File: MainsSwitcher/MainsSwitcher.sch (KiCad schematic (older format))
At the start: 25 parts, among them J1 SERIAL, J2 LED_STRIP, J3 SWITCHING, J4 MAINS_IN, J5 TEMP_SEN1, J6 TEMP_SEN2, K1 Relay, P1 GPIO, Q1 MOSFET_N, Q2 MCP1700T-3302E/TT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

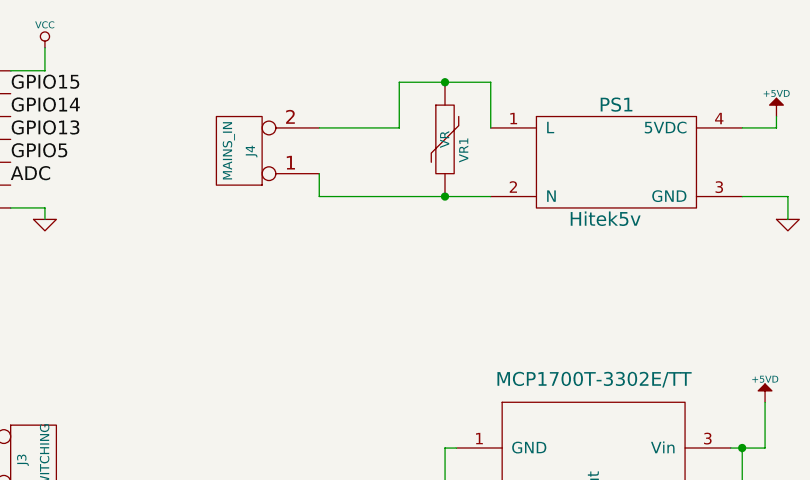
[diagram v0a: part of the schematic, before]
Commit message: Added fuseholder
Fuseholder added to the mains inlet. As ordered.
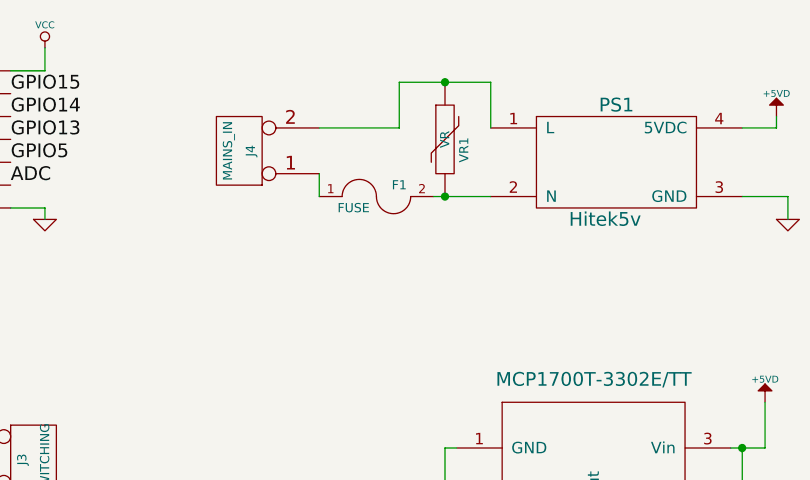
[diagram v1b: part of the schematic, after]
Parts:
- added F1: FUSE, TJS:Schurter_Fuseholder(20x5mm)0031.8211, symbol FUSE
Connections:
- net at PS1.2 (N), VR1.2: now also F1.2; no longer J4.1 (P1)
- new net: F1.1, J4.1 (P1)
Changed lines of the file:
@@
 Connection ~ 8900 850
 Connection ~ 8900 1350
-Wire Wire Line
-	8350 1350 9100 1350
 $Comp
 L +5VD #PWR028
@@
 Wire Wire Line
 	6600 5300 6600 5450
+$Comp
+L FUSE F1
+U 1 1 58B4A8B2
+P 8600 1350
+F 0 "F1" H 8700 1400 40  0000 C CNN
+F 1 "FUSE" H 8500 1300 40  0000 C CNN
+F 2 "TJS:Schurter_Fuseholder(20x5mm)0031.8211" H 8600 1350 60  0001 C CNN
+F 3 "" H 8600 1350 60  0000 C CNN
+	1    8600 1350
+	1    0    0    -1
+$EndComp
+Wire Wire Line
+	8850 1350 9100 1350
 $EndSCHEMATC

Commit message: Changes to who knows what.
Uncommitted changes to stuff. Tidying up…
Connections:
- net GND: now also U1.10 (GPIO15)
- net VCC: now also P1.6 (P6)
- removed net GPIO15: P1.6 (P6), U1.10 (GPIO15)
- net GPIO5 renamed GPIO4
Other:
- note added: "Note:\nGPIO4 and GPIO5 are swapped\n on the original part net for the \nESP8266."
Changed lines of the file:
@@
 GPIO13
 Text Label 3100 3000 0    60   ~ 0
-GPIO5
+GPIO4
 Text Label 3100 3800 0    60   ~ 0
 ADC
@@
 ADC
 Text Label 7000 1200 0    60   ~ 0
-GPIO5
+GPIO4
 Text Label 7000 1100 0    60   ~ 0
 GPIO13
 Text Label 7000 1000 0    60   ~ 0
 GPIO14
-Text Label 7000 900  0    60   ~ 0
-GPIO15
 Wire Wire Line
 	7150 800  7000 800
@@
 $EndComp
 Wire Wire Line
-	7150 700  7150 800
+	7150 700  7150 900
 Wire Wire Line
 	8450 5100 8450 5050
@@
 	6600 4250 6250 4250
 Text Label 6250 4250 0    60   ~ 0
-GPIO5
+GPIO4
 Wire Wire Line
 	6600 5300 6600 5450
@@
 Wire Wire Line
 	8850 1350 9100 1350
+$Comp
+L GND #PWR?
+U 1 1 59711544
+P 3600 2250
+F 0 "#PWR?" H 3600 2250 30  0001 C CNN
+F 1 "GND" H 3600 2180 30  0001 C CNN
+F 2 "" H 3600 2250 60  0001 C CNN
+F 3 "" H 3600 2250 60  0001 C CNN
+	1    3600 2250
+	1    0    0    -1
+$EndComp
+Wire Wire Line
+	3600 2250 3600 2200
+Wire Wire Line
+	3600 2200 3100 2200
+Text Notes 1750 4450 0    60   ~ 0
+Note:\nGPIO4 and GPIO5 are swapped\n on the original part net for the \nESP8266.
+Wire Wire Line
+	7150 900  7000 900
+Connection ~ 7150 800
 $EndSCHEMATC
